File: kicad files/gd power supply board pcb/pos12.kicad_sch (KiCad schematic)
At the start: 29 parts, among them Q2 BC817, Q3 MMBT3906, Q4 FDS9435A, U2 mc34063

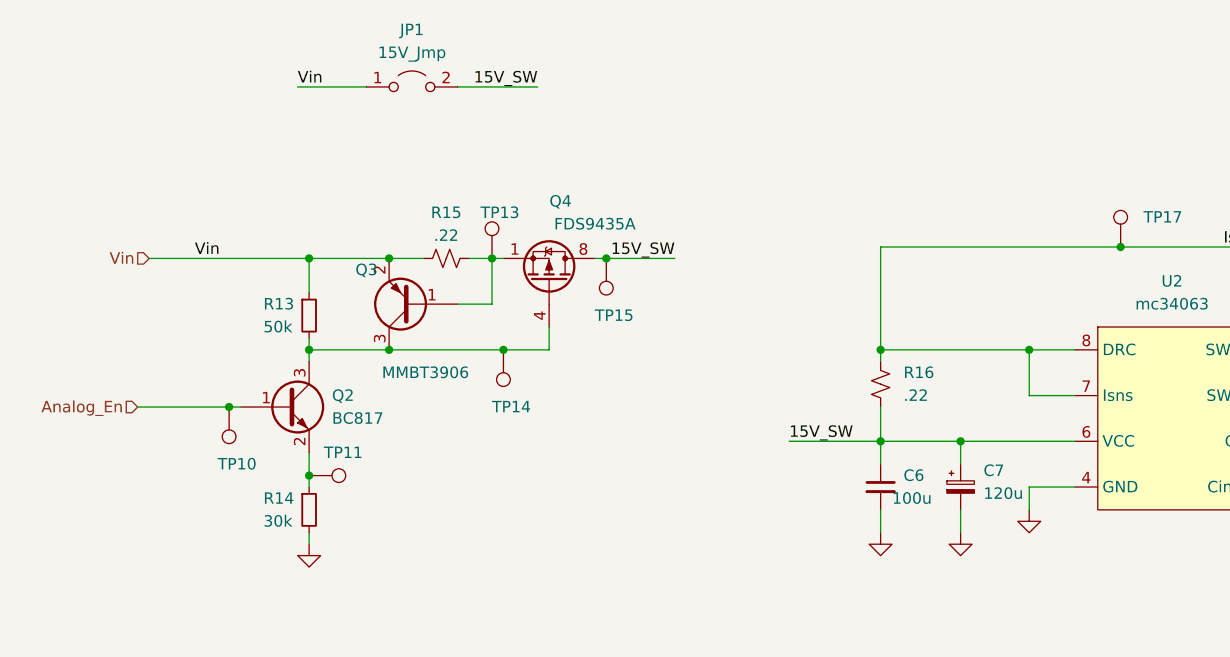
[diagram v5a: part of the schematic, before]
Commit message: notes for power supply board added to schematic
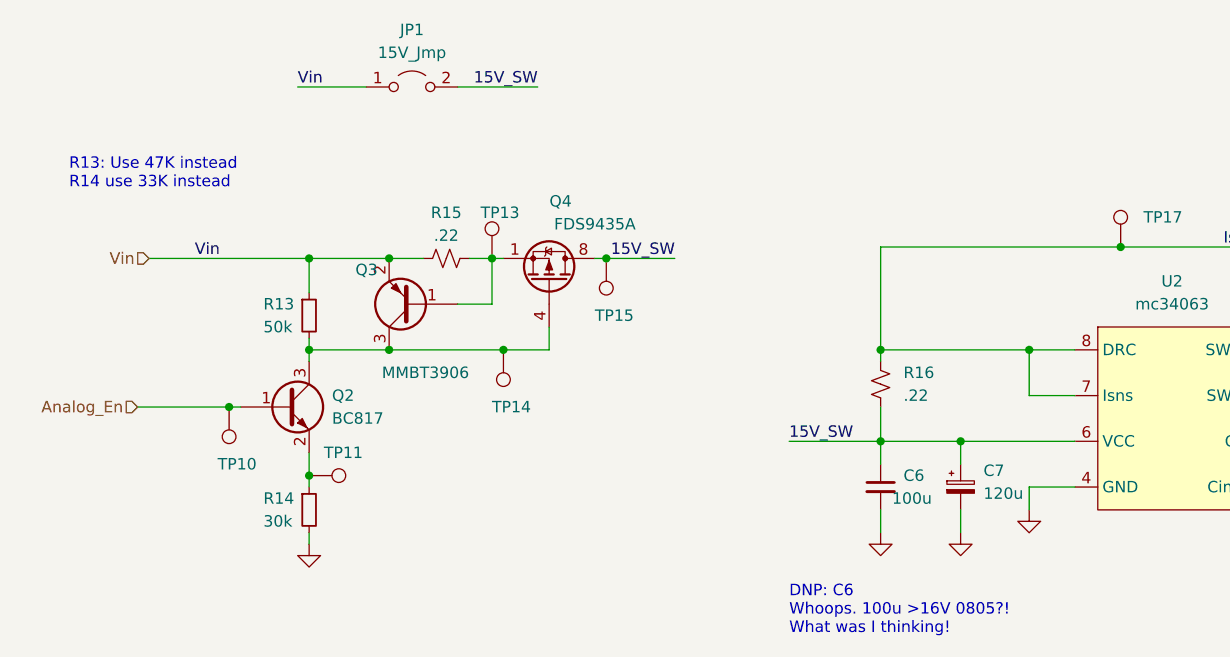
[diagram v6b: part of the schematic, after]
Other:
- note added: "DNP: C6 Whoops. 100u >16V 0805?! What was I thinking!"
- note added: "R13: Use 47K instead R14 use 33K instead"
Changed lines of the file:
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@@
     (stroke (width 0) (type default) (color 0 0 0 0))
+  )
+  (text "DNP: C6\nWhoops. 100u >16V 0805?!\nWhat was I thinking!"
+    (at 107.95 121.92 0)
+    (effects (font (size 1.27 1.27)) (justify left bottom))
+  )
+  (text "R13: Use 47K instead\nR14 use 33K instead" (at 27.94 72.39 0)
+    (effects (font (size 1.27 1.27)) (justify left bottom))
   )
   (label "Isense" (at 156.21 78.74 0)

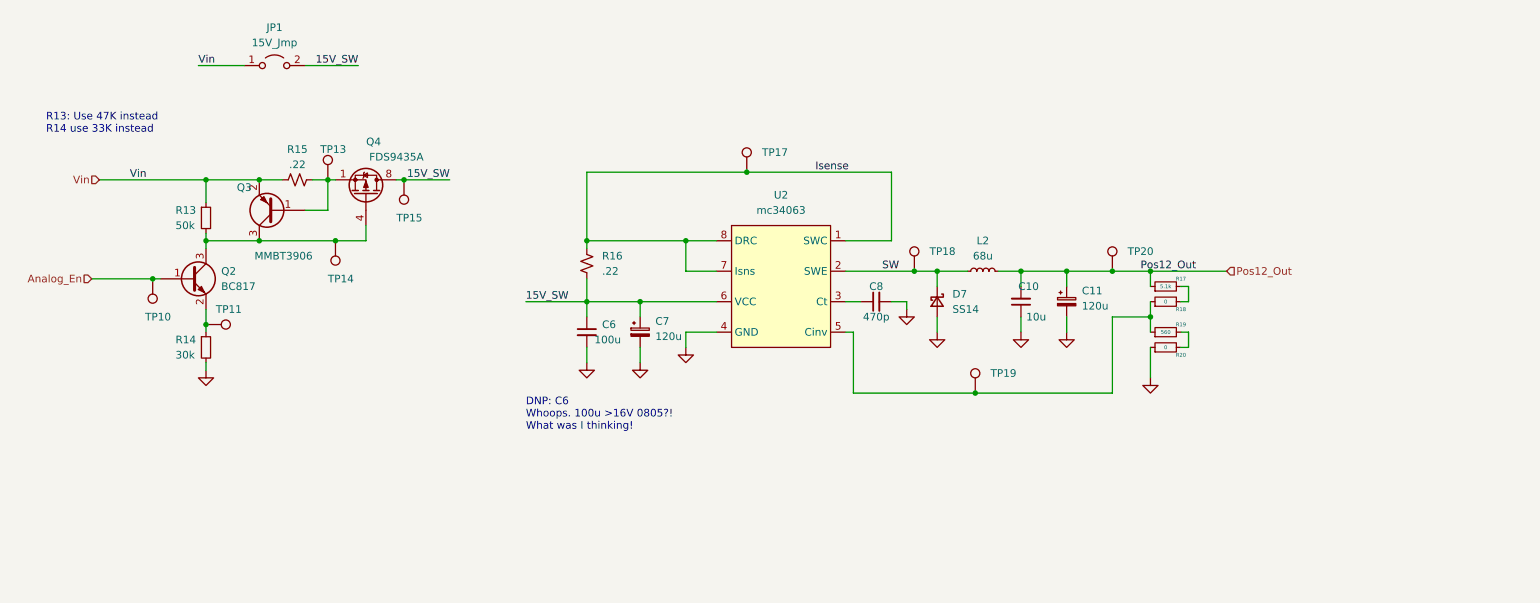
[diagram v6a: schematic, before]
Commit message: added filters and ripped up the board
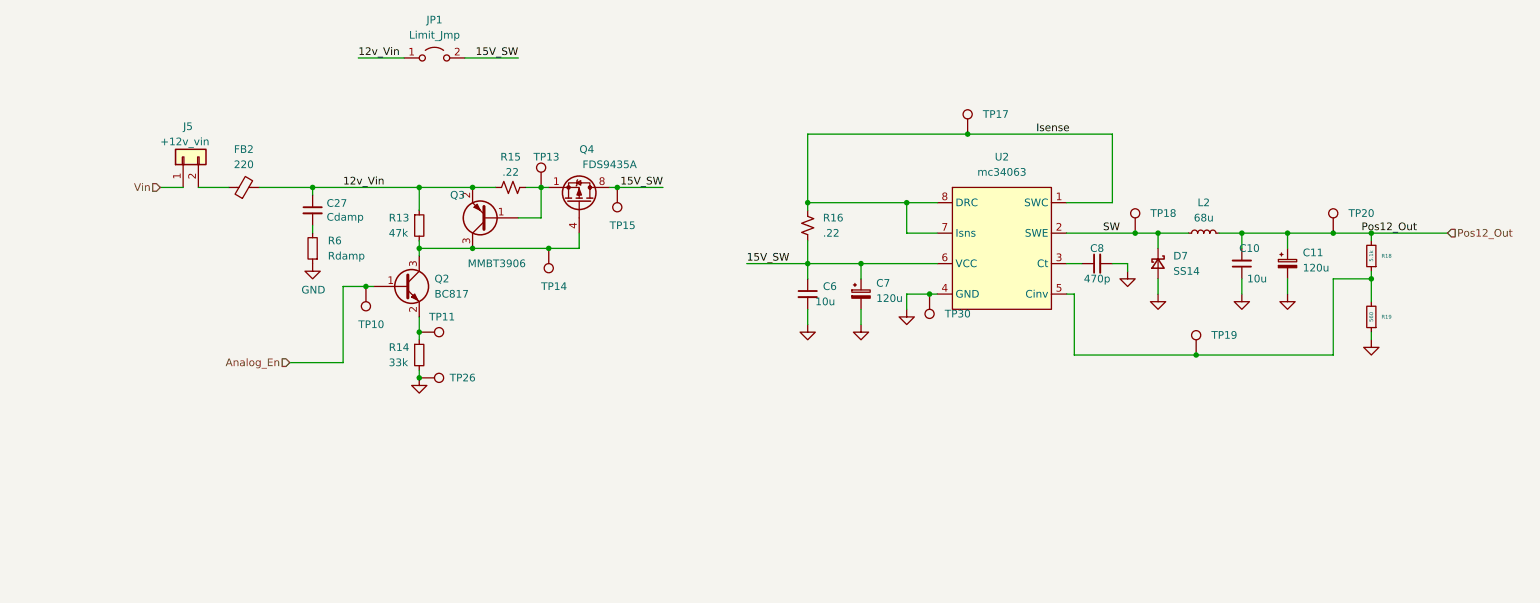
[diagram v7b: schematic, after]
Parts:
- removed R17, R20: 0, Resistor_SMD:R_0805_2012Metric, symbol My Library:R_0805
- added C27: Cdamp, Capacitor_SMD:C_0805_2012Metric_Pad1.18x1.45mm_HandSolder, symbol Device:C_Small
- added FB2: 220, Inductor_SMD:L_0603_1608Metric_Pad1.05x0.95mm_HandSolder, symbol Device:FerriteBead_Small
- added J5: +12v_vin, Connector_PinHeader_2.54mm:PinHeader_1x02_P2.54mm_Vertical, symbol Connector_Generic:Conn_01x02
- added R6: Rdamp, Resistor_SMD:R_0805_2012Metric_Pad1.20x1.40mm_HandSolder, symbol My Library:R_0805
- added TP26, TP30: TestPoint_Harwin, TestPoint:TestPoint_Pad_1.0x1.0mm, symbol My Library:TestPoint_Harwin
- C6: value 100u -> 10u
- JP1: value 15V_Jmp -> Limit_Jmp
- R13: value 50k -> 47k
- R14: value 30k -> 33k
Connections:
- net GND: now also R19.1, R6.1, TP26.1, TP30.1
- net Pos12_Out: now also R18.2
- net Vin: now also J5.1 (Pin_1); no longer JP1.1 (A), Q3.2 (E), R13.1, R15.1
- net at R18.1, TP19.1, U2.5 (Cinv): now also R19.2; no longer R19.1
- new net: FB2.1, J5.2 (Pin_2)
- new net: C27.2, R6.2
- new net 12v_Vin: C27.1, FB2.2, JP1.1 (A), Q3.2 (E), R13.1, R15.1
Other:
- note removed: "DNP: C6 Whoops. 100u >16V 0805?! What was I thinking!"
- note removed: "R13: Use 47K instead R14 use 33K instead"
- moved on the sheet: C10, C11, C6, C7, C8, D7, JP1, L2, Q2, Q3, Q4, R13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

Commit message: rev2 - round 1
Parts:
- added R2: 10K, Resistor_SMD:R_0805_2012Metric, symbol Device:R_Small
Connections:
- net Analog_En: now also R2.1
- net GND: now also R2.2
- net SW renamed +12V_SW
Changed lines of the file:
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@@
   (junction (at 242.57 88.9) (diameter 0) (color 0 0 0 0)
   )
+  (junction (at 73.66 110.49) (diameter 0) (color 0 0 0 0)
+  )
   (junction (at 163.83 93.98) (diameter 0) (color 0 0 0 0)
   )
@@
     (stroke (width 0) (type default) (color 0 0 0 0))
   )
+  (wire (pts (xy 73.66 110.49) (xy 77.47 110.49))
+    (stroke (width 0) (type default) (color 0 0 0 0))
+  )
   (wire (pts (xy 90.17 81.28) (xy 90.17 85.09))
     (stroke (width 0) (type default) (color 0 0 0 0))
@@
     (stroke (width 0) (type default) (color 0 0 0 0))
   )
-  (wire (pts (xy 68.58 110.49) (xy 77.47 110.49))
+  (wire (pts (xy 68.58 110.49) (xy 73.66 110.49))
     (stroke (width 0) (type default) (color 0 0 0 0))
   )
@@
     (effects (font (size 1.27 1.27)) (justify right bottom))
   )
-  (label "SW" (at 207.01 88.9 180)
+  (label "+12V_SW" (at 207.01 88.9 180)
     (effects (font (size 1.27 1.27)) (justify right bottom))
   )
@@
     (pin "1")
   )
+  (symbol (lib_id "power:GND") (at 73.66 115.57 0) (unit 1)
+    (in_bom yes) (on_board yes) (fields_autoplaced)
+    (property "Reference" "#PWR0101" (id 0) (at 73.66 121.92 0)
+      (effects (font (size 1.27 1.27)) hide)
+    )
+    (property "Value" "GND" (id 1) (at 73.66 120.65 0)
+      (effects (font (size 1.27 1.27)) hide)
+    )
+    (property "Footprint" "" (id 2) (at 73.66 115.57 0)
+      (effects (font (size 1.27 1.27)) hide)
+    )
+    (property "Datasheet" "" (id 3) (at 73.66 115.57 0)
+      (effects (font (size 1.27 1.27)) hide)
+    )
+    (pin "1")
+  )
   (symbol (lib_id "power:GND") (at 248.92 106.68 0) (unit 1)
     (in_bom yes) (on_board yes) (fields_autoplaced)
@@
       (effects (font (size 1.27 1.27)) hide)
     )
+    (pin "1")
+    (pin "2")
+  )
+  (symbol (lib_id "Device:R_Small") (at 73.66 113.03 0) (unit 1)
+    (in_bom yes) (on_board yes)
+    (property "Reference" "R2" (id 0) (at 68.58 111.76 0)
+      (effects (font (size 1.27 1.27)) (justify left))
+    )
+    (property "Value" "10K" (id 1) (at 68.58 114.3 0)
+      (effects (font (size 1.27 1.27)) (justify left))
+    )
+    (property "Footprint" "Resistor_SMD:R_0805_2012Metric" (id 2) (at 73.66 113.03 0)
+      (effects (font (size 1.27 1.27)) hide)
+    )
+    (property "Datasheet" "~" (id 3) (at 73.66 113.03 0)
+      (effects (font (size 1.27 1.27)) hide)
+    )
